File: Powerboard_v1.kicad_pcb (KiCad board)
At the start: 2 copper layers, 84.5 x 51.7 mm, 51 parts, among them IC1 LM339N, IC2 MMBT3904, IC3 TPS563200DDCR, IC4 LM25145RGYR, J1 Conn_01x05_Pin, J2 Conn_01x02_Socket, J4 1.5 mm, J5 1.5 mm, Q3 35A, 30V, Q4 35A Id, 30V Vds

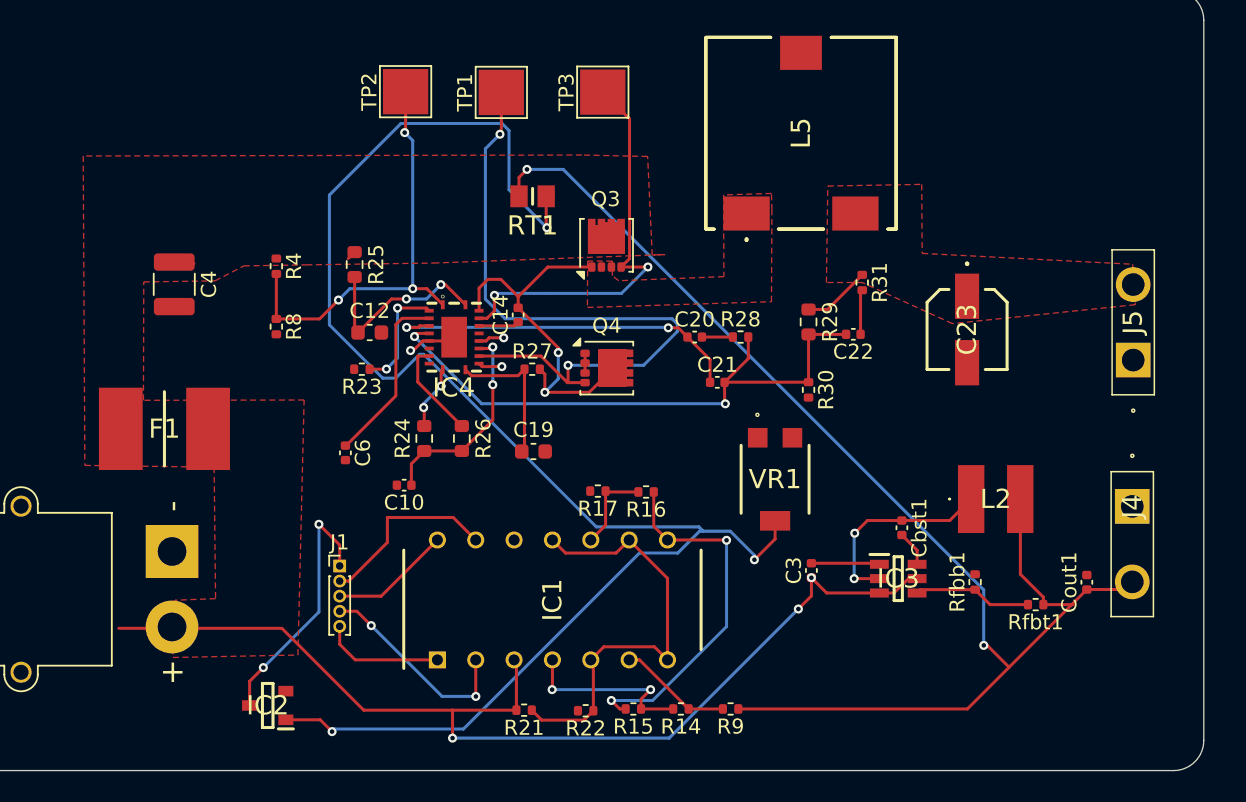
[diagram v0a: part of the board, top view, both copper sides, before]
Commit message: corrected version with better connections for high power
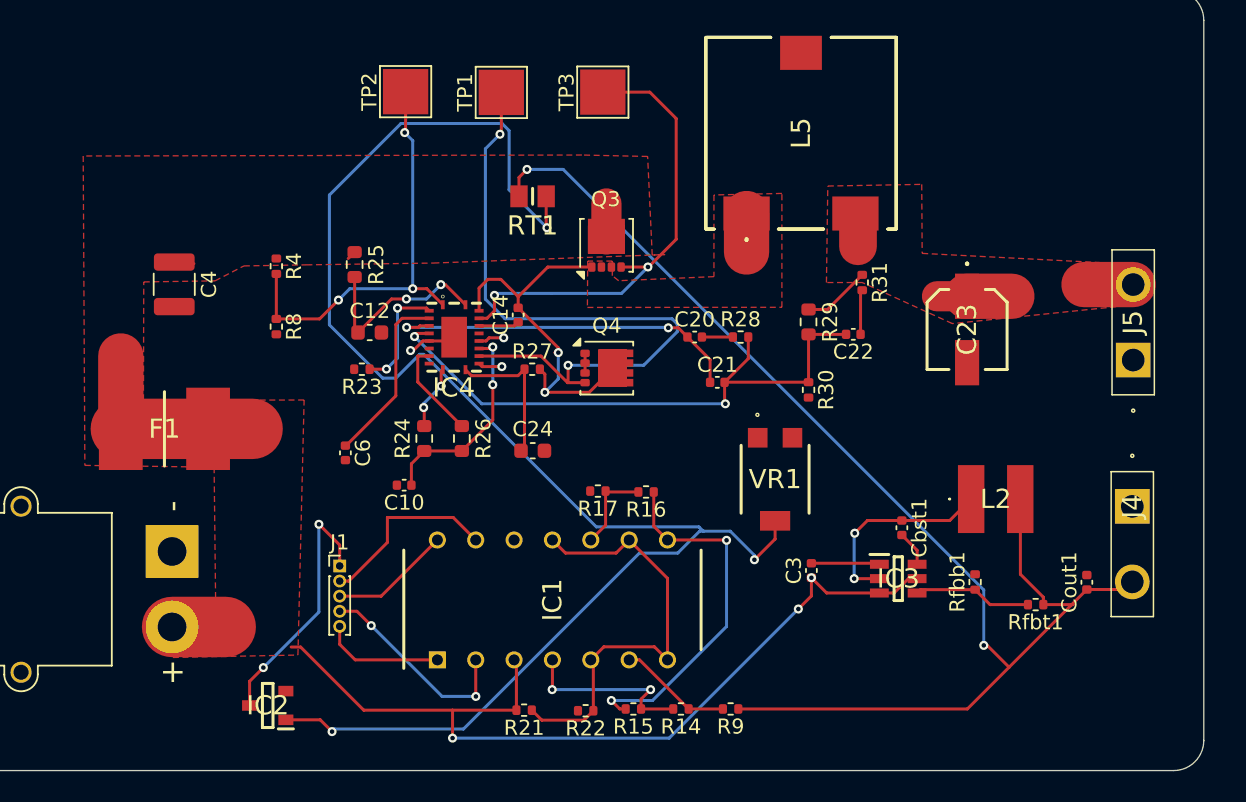
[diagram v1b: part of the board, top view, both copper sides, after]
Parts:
- removed C19: 10pF 100Vdc, Capacitor_SMD:C_0603_1608Metric
- added C24: 10pF 100Vdc, Capacitor_SMD:C_0603_1608Metric, F.Cu at (146.0, 123.5)
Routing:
- net Net-(C23-+): track 6.99 -> 18.2 mm
- net Batt +: track 74.5 -> 81.6 mm
- net Net-(IC4-HO): track 27.5 -> 31.2 mm
- net Net-(IC4-SW): track 25.7 -> 28.4 mm

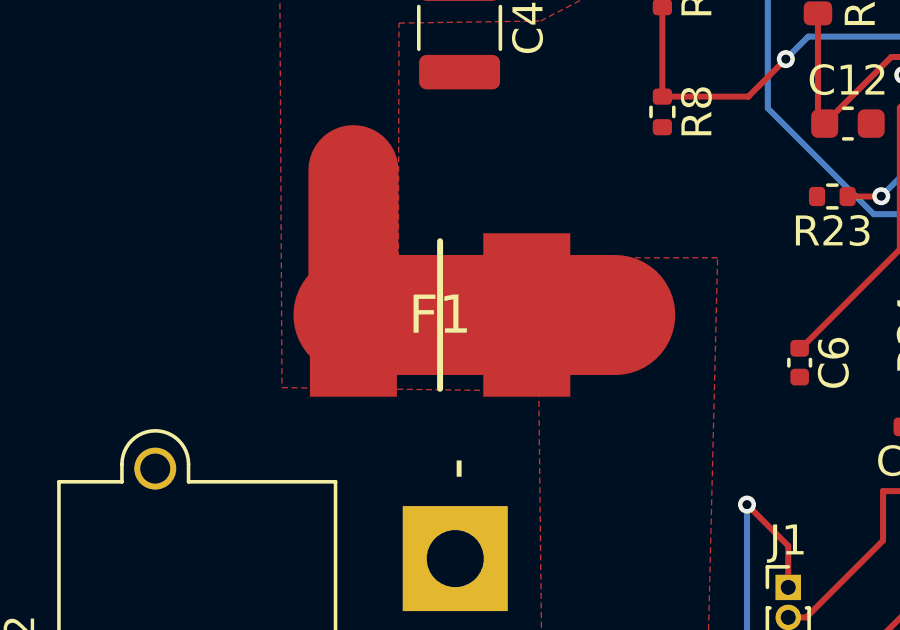
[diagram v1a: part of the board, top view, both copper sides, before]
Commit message: Corrected fuse footprint
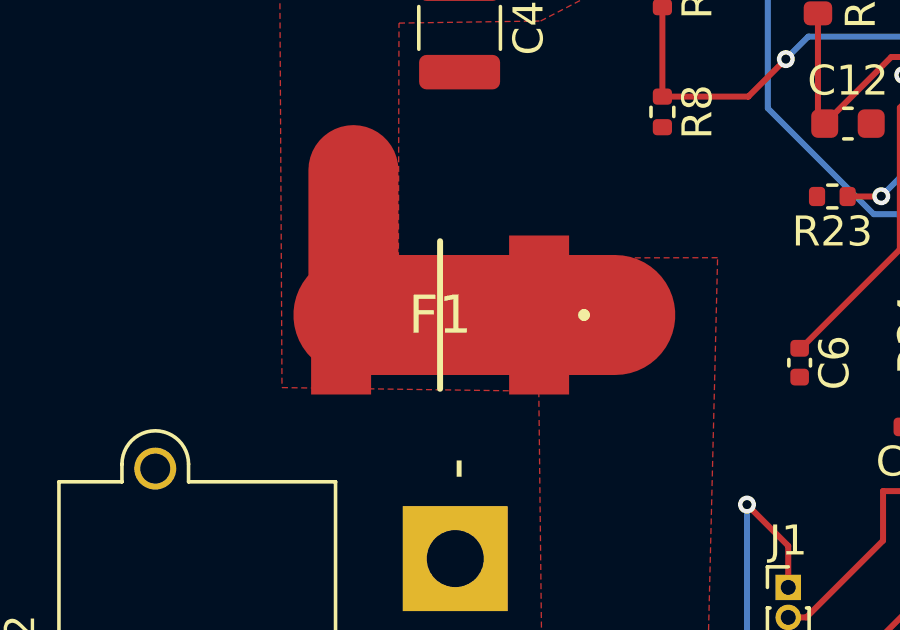
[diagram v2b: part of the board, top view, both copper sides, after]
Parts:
- F1: footprint Powerboard:FUSC7451X160N -> Powerboard:2920L07560MR
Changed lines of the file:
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@@
 		)
 	)
-	(footprint "Powerboard:FUSC7451X160N"
+	(footprint "Powerboard:2920L07560MR"
 		(layer "F.Cu")
 		(at 121.61 122.05 180)
-		(descr "2920L600/12")
+		(descr "2920L075")
 		(tags "Resettable Fuse")
 		(property "Reference" "F1"
-			(at 0 0 0)
+			(at 0 0 180)
 			(layer "F.SilkS")
 			(effects
@@
 		)
 		(property "Value" "Fuse"
-			(at 0 0 0)
+			(at 0 0 180)
 			(layer "F.SilkS")
 			(hide yes)
@@
 		)
 		(property "Datasheet" ""
-			(at 0 0 0)
+			(at 0 0 180)
 			(layer "F.Fab")
 			(hide yes)
@@
 		)
 		(property "Description" "Fuse"
-			(at 0 0 0)
+			(at 0 0 180)
 			(layer "F.Fab")
 			(hide yes)
@@
 		)
 		(fp_line
-			(start 4.59 2.975)
-			(end -4.59 2.975)
-			(stroke
-				(width 0.05)
-				(type solid)
-			)
-			(layer "F.CrtYd")
-		)
-		(fp_line
-			(start 4.59 -2.975)
-			(end 4.59 2.975)
-			(stroke
-				(width 0.05)
-				(type solid)
-			)
-			(layer "F.CrtYd")
-		)
-		(fp_line
-			(start -4.59 2.975)
-			(end -4.59 -2.975)
-			(stroke
-				(width 0.05)
-				(type solid)
-			)
-			(layer "F.CrtYd")
-		)
-		(fp_line
-			(start -4.59 -2.975)
-			(end 4.59 -2.975)
-			(stroke
-				(width 0.05)
+			(start -4.8 0.1)
+			(end -4.8 0.1)
+			(stroke
+				(width 0.2)
+				(type solid)
+			)
+			(layer "F.SilkS")
+		)
+		(fp_line
+			(start -4.8 -0.1)
+			(end -4.8 -0.1)
+			(stroke
+				(width 0.2)
+				(type solid)
+			)
+			(layer "F.SilkS")
+		)
+		(fp_arc
+			(start -4.8 0.1)
+			(mid -4.9 0)
+			(end -4.8 -0.1)
+			(stroke
+				(width 0.2)
+				(type solid)
+			)
+			(layer "F.SilkS")
+		)
+		(fp_arc
+			(start -4.8 -0.1)
+			(mid -4.7 0)
+			(end -4.8 0.1)
+			(stroke
+				(width 0.2)
+				(type solid)
+			)
+			(layer "F.SilkS")
+		)
+		(fp_line
+			(start 5.3 3.65)
+			(end -5.3 3.65)
+			(stroke
+				(width 0.1)
+				(type solid)
+			)
+			(layer "F.CrtYd")
+		)
+		(fp_line
+			(start 5.3 -3.65)
+			(end 5.3 3.65)
+			(stroke
+				(width 0.1)
+				(type solid)
+			)
+			(layer "F.CrtYd")
+		)
+		(fp_line
+			(start -5.3 3.65)
+			(end -5.3 -3.65)
+			(stroke
+				(width 0.1)
+				(type solid)
+			)
+			(layer "F.CrtYd")
+		)
+		(fp_line
+			(start -5.3 -3.65)
+			(end 5.3 -3.65)
+			(stroke
+				(width 0.1)
 				(type solid)
 			)
@@
 		)
 		(fp_text user "${REFERENCE}"
-			(at 0 0 0)
+			(at 0 0 180)
 			(layer "F.Fab")
 			(effects
@@
 		)
 		(pad "1" smd rect
-			(at -2.89 0 180)
-			(size 2.9 5.45)
+			(at -3.3 0 180)
+			(size 2 5.3)
 			(layers "F.Cu" "F.Mask" "F.Paste")
 			(net 2 "Batt +")
@@
 		)
 		(pad "2" smd rect
-			(at 2.89 0 180)
-			(size 2.9 5.45)
+			(at 3.3 0 180)
+			(size 2 5.3)
 			(layers "F.Cu" "F.Mask" "F.Paste")
 			(net 2 "Batt +")
@@
 		)
 		(embedded_fonts no)
-		(model "2920L600_16MR.stp"
+		(model "2920L700_12MR.stp"
 			(offset
-				(xyz 0 0 0)
+				(xyz 0 0 2.719999988)
 			)
 			(scale
